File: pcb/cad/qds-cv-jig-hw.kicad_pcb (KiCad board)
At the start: 2 copper layers, 13 parts, among them J1 Conn_02x01, J10 Conn_02x01, J11 Conn_02x01, J12 Conn_01x02, J13 Conn_02x01, J2 Conn_01x02, J3 Conn_02x01, J4 Conn_02x01, J5 Conn_01x02, J6 Conn_02x01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

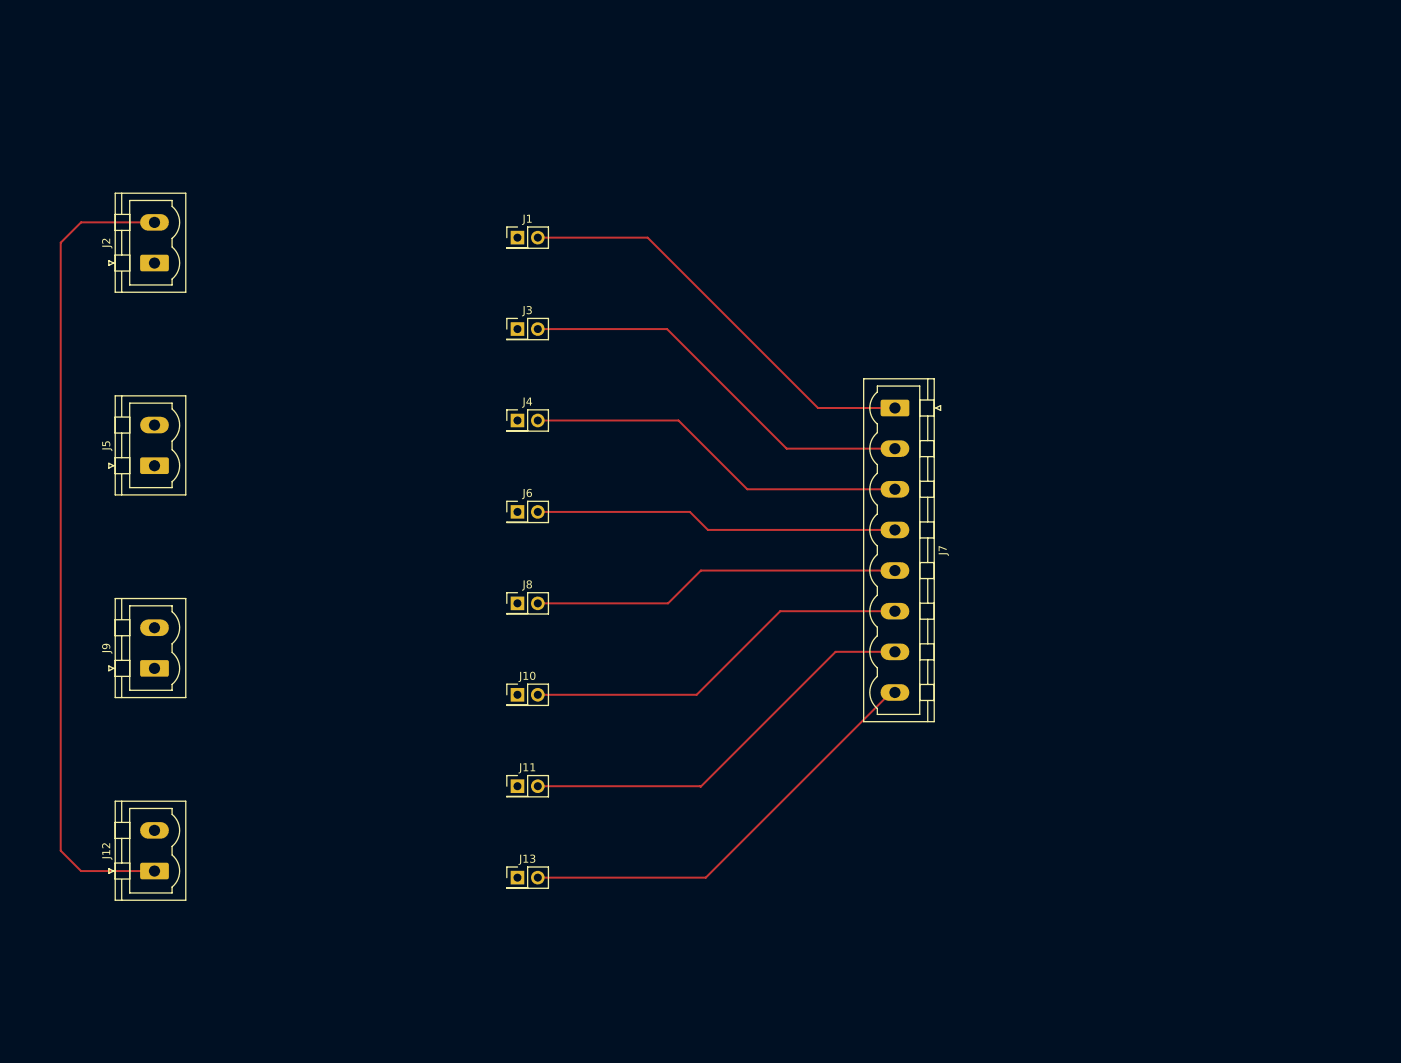
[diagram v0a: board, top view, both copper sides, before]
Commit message: Include connectors, jumpers, tracks and mounting holes on schematics and PCB
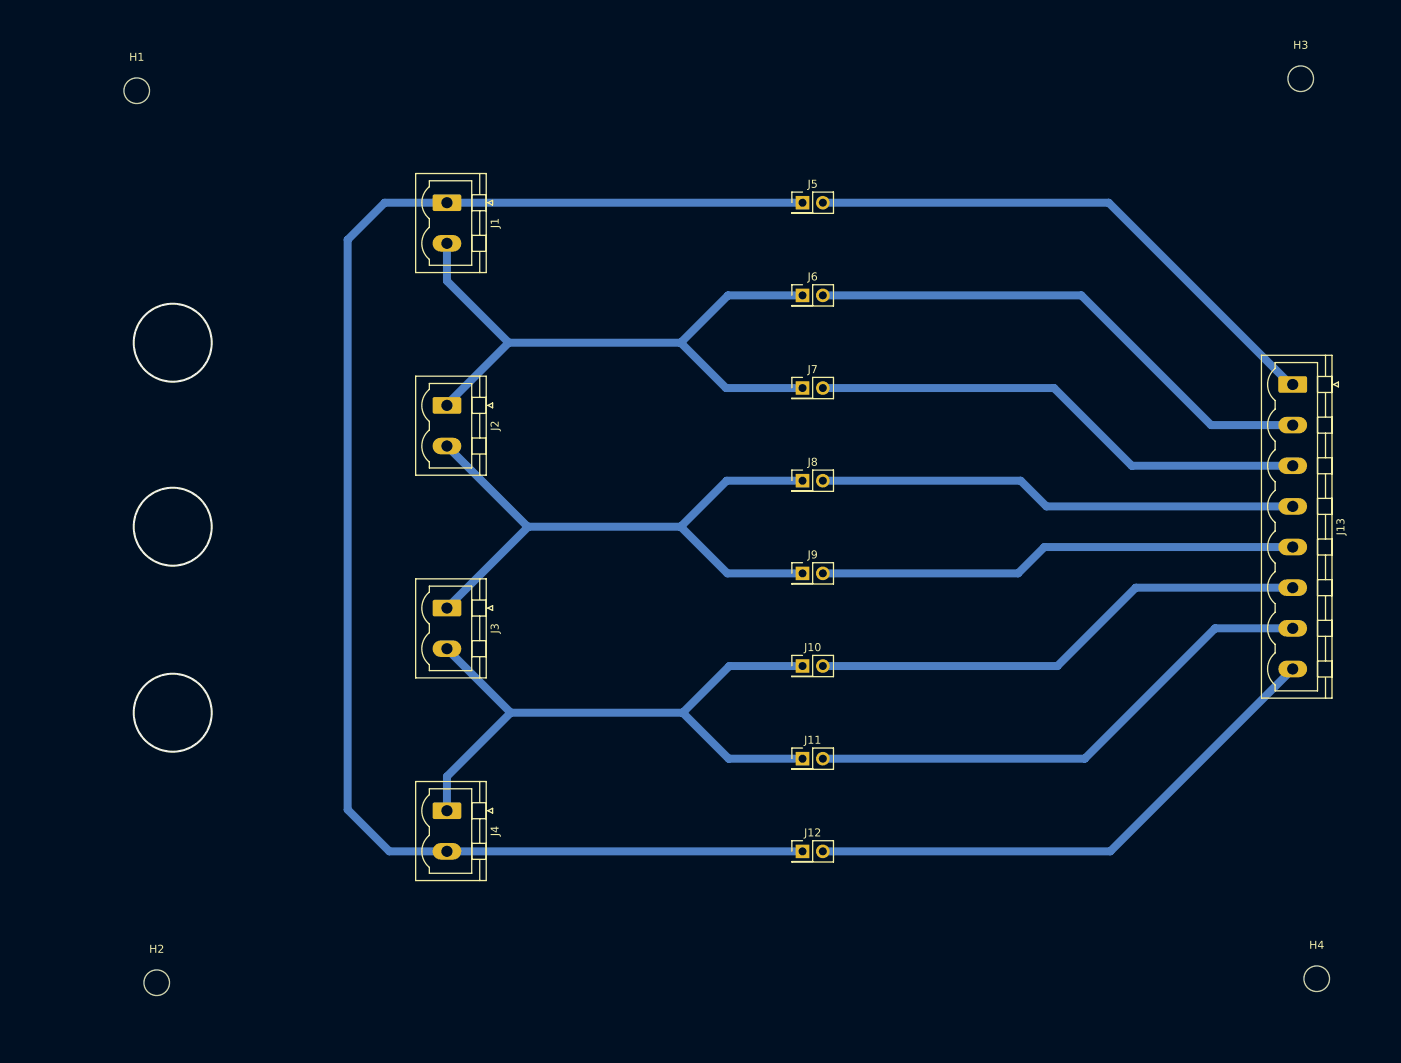
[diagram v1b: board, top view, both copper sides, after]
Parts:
- added H1: MountingHole, MountingHole:MountingHole_3.2mm_M3, F.Cu at (75.5, 43.0)
- added H2: MountingHole, MountingHole:MountingHole_3.2mm_M3, F.Cu at (78.0, 154.5)
- added H3: MountingHole, MountingHole:MountingHole_3.2mm_M3, F.Cu at (221.0, 41.5)
- added H4: MountingHole, MountingHole:MountingHole_3.2mm_M3, F.Cu at (223.0, 154.0)
- J1, J3, J4: value Conn_02x01 -> Conn_01x02; footprint Connector_PinHeader_2.54mm:PinHeader_2x01_P2.54mm_Vertical -> Connector_Phoenix_MSTB:PhoenixContact_MSTBVA_2,5_2-G-5,08_1x02_P5.08mm_Vertical
- J12, J5, J9: value Conn_01x02 -> Conn_02x01; footprint Connector_Phoenix_MSTB:PhoenixContact_MSTBVA_2,5_2-G-5,08_1x02_P5.08mm_Vertical -> Connector_PinHeader_2.54mm:PinHeader_2x01_P2.54mm_Vertical
- J13: value Conn_02x01 -> Conn_01x08; footprint Connector_PinHeader_2.54mm:PinHeader_2x01_P2.54mm_Vertical -> Connector_Phoenix_MSTB:PhoenixContact_MSTBVA_2,5_8-G-5,08_1x08_P5.08mm_Vertical
- J7: value Conn_01x08 -> Conn_02x01; footprint Connector_Phoenix_MSTB:PhoenixContact_MSTBVA_2,5_8-G-5,08_1x08_P5.08mm_Vertical -> Connector_PinHeader_2.54mm:PinHeader_2x01_P2.54mm_Vertical
- moved J13 114.9 mm to (220.0, 79.7), turned to -90 degrees
- moved J5 87.4 mm to (158.7, 57.0), turned to 0 degrees
- moved J9 81.9 mm to (158.7, 103.3), turned to 0 degrees
- moved J12 81.0 mm to (158.7, 138.1), turned to 0 degrees
- moved J4 49.6 mm to (114.3, 133.0), turned to -90 degrees
- moved J6 44.7 mm to (158.7, 68.6)
- moved J2 40.7 mm to (114.3, 82.3), turned to -90 degrees
- moved J8 38.8 mm to (158.7, 91.7)
- moved J3 36.0 mm to (114.3, 107.7), turned to -90 degrees
- moved J10 35.8 mm to (158.7, 114.9)
- moved J11 35.8 mm to (158.7, 126.5)
- moved J7 11.8 mm to (158.7, 80.2), turned to 0 degrees
- moved J1 9.84 mm to (114.3, 57.0), turned to -90 degrees
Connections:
- J1 pad 1: Net-(J1-Pad1) -> Net-(J5-Pad1)
- J1 pad 2: Net-(J1-Pad2) -> Net-(J6-Pad1)
- J12 pad 1: Net-(J1-Pad1) -> Net-(J5-Pad1)
- J12 pad 2: Net-(J10-Pad1) -> Net-(J12-Pad2)
- J13 pad 1: Net-(J1-Pad1) -> Net-(J5-Pad2)
- J13 pad 2: Net-(J13-Pad2) -> Net-(J6-Pad2)
- J2 pad 1: Net-(J2-Pad1) -> Net-(J6-Pad1)
- J2 pad 2: Net-(J1-Pad1) -> Net-(J8-Pad1)
- J3 pad 1: Net-(J2-Pad1) -> Net-(J8-Pad1)
- J3 pad 2: Net-(J3-Pad2) -> Net-(J10-Pad1)
- J4 pad 1: Net-(J2-Pad1) -> Net-(J10-Pad1)
- J4 pad 2: Net-(J4-Pad2) -> Net-(J5-Pad1)
- J5 pad 2: Net-(J2-Pad1) -> Net-(J5-Pad2)
- J6 pad 1: Net-(J5-Pad1) -> Net-(J6-Pad1)
- J7 pad 1: Net-(J1-Pad2) -> Net-(J6-Pad1)
- J7 pad 2: Net-(J3-Pad2) -> Net-(J7-Pad2)
- J8 pad 1: Net-(J5-Pad1) -> Net-(J8-Pad1)
- J8 pad 2: Net-(J7-Pad5) -> Net-(J8-Pad2)
- J9 pad 1: Net-(J10-Pad1) -> Net-(J8-Pad1)
- J9 pad 2: Net-(J5-Pad1) -> Net-(J13-Pad5)
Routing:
- net Net-(J5-Pad1): track 0.00 -> 189.0 mm
- net Net-(J1-Pad1): track 101.5 -> 0.00 mm
- net Net-(J6-Pad1): track 0.00 -> 83.4 mm
- net Net-(J8-Pad1): track 0.00 -> 83.3 mm
- net Net-(J10-Pad1): track 0.00 -> 83.1 mm
- net Net-(J12-Pad2): track 0.00 -> 68.2 mm
- net Net-(J5-Pad2): track 0.00 -> 68.1 mm
- net Net-(J7-Pad2): track 0.00 -> 63.1 mm
- net Net-(J13-Pad5): track 0.00 -> 60.1 mm
- net Net-(J8-Pad2): track 0.00 -> 60.1 mm
- net Net-(J13-Pad2): track 54.2 -> 0.00 mm
- net Net-(J1-Pad2): track 53.5 -> 0.00 mm
- net Net-(J3-Pad2): track 50.8 -> 0.00 mm
- net Net-(J4-Pad2): track 48.2 -> 0.00 mm
- net Net-(J7-Pad5): track 46.3 -> 0.00 mm
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
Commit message: Include board outline, potentiometer and spacers, place GND fill
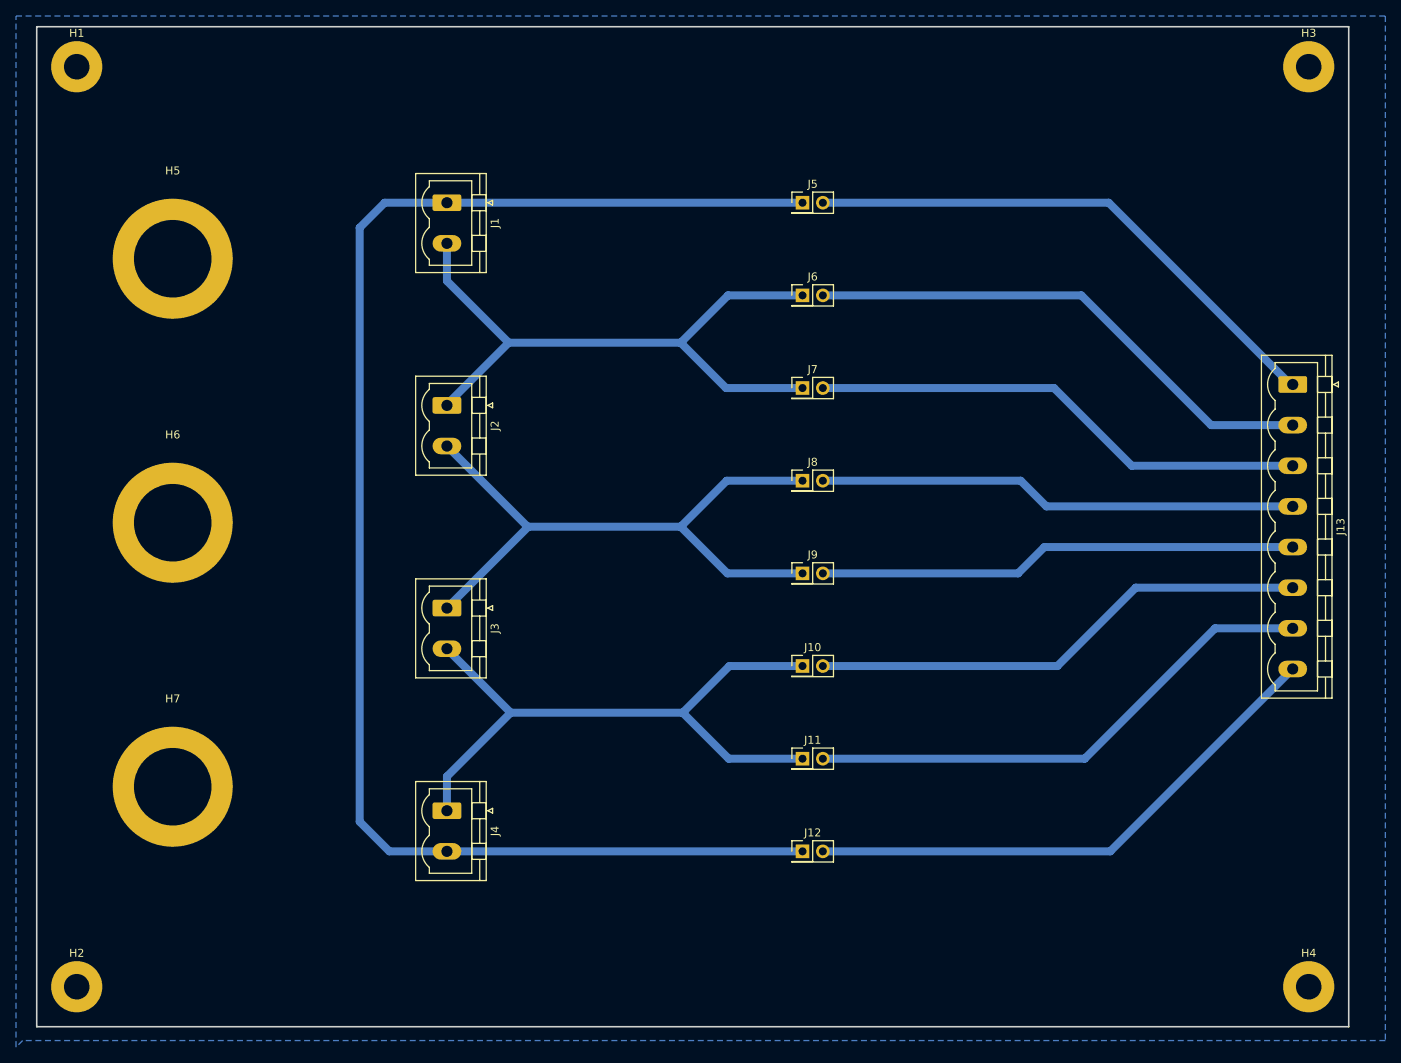
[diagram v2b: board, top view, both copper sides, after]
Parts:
- added H5: MountingHole, qds-cv-jig-hw-lib:Potentiometer_Vishay_534, F.Cu at (80.0, 64.0)
- added H6: MountingHole, qds-cv-jig-hw-lib:Potentiometer_Vishay_534, F.Cu at (80.0, 97.0)
- added H7: MountingHole, qds-cv-jig-hw-lib:Potentiometer_Vishay_534, F.Cu at (80.0, 130.0)
- H1, H2, H3, H4: footprint MountingHole:MountingHole_3.2mm_M3 -> MountingHole:MountingHole_3.2mm_M3_Pad
- moved H2 10.0 mm to (68.0, 155.0)
- moved H1 8.08 mm to (68.0, 40.0)
- moved H3 1.80 mm to (222.0, 40.0)
- moved H4 1.41 mm to (222.0, 155.0)
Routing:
- net Net-(J1-Pad1): track 189.0 -> 187.8 mm
- net (no net): vias 3 -> 0
- added copper zone on B.Cu, net GND
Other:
- board outline added: 164 x 125 mm
